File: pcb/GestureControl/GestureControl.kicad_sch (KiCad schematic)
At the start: 71 parts, among them J1 Conn_01x04_I2I-LCD, J2 BATT, J3 Conn_01x08, J4 Conn_01x06, J5 Conn_01x10, J6 Conn_01x08, SW1 SW1, SW2 SW2, U1 AP5100_3.3, U2 AP5100_3.3

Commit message: add breakoutboard
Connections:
- net GPIOI_0: now also J5.2 (Pin_2); no longer J5.3 (Pin_3)
- net GPIOI_1: now also J5.3 (Pin_3); no longer J5.4 (Pin_4)
- net GPIOI_2: now also J5.4 (Pin_4); no longer J5.5 (Pin_5)
- net GPIOI_3: now also J5.5 (Pin_5); no longer J5.6 (Pin_6)
- net XSHUT_0: now also J3.8 (Pin_8); no longer J4.1 (Pin_1)
- net XSHUT_1: now also J4.1 (Pin_1); no longer J4.2 (Pin_2)
- net XSHUT_2: now also J4.2 (Pin_2); no longer J4.3 (Pin_3)
- net XSHUT_3: now also J4.3 (Pin_3); no longer J4.4 (Pin_4)
- new net GPIOI_4: J5.6 (Pin_6)
- new net XSHUT_4: J4.4 (Pin_4)

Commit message: add docs
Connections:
- net LED_5 is gone; now on net LED_4: J6.3 (Pin_3), R5.2
- net LED_1: now also J6.6 (Pin_6), R2.2; no longer J6.7 (Pin_7), R1.2
- net LED_2: now also J6.5 (Pin_5), R3.2; no longer J6.6 (Pin_6), R2.2
- net LED_3: now also J6.4 (Pin_4), R4.2; no longer J6.5 (Pin_5), R3.2
- net LED_4: no longer J6.4 (Pin_4), R4.2
- new net LED_0: J6.7 (Pin_7), R1.2
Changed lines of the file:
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@@
     )
   )
-  (global_label "LED_1" (shape input) (at 26.67 31.75 180) (fields_autoplaced)
+  (global_label "LED_0" (shape input) (at 26.67 31.75 180) (fields_autoplaced)
     (effects (font (size 1.27 1.27)) (justify right))
-    (property "Intersheet References" "${INTERSHEET_REFS}" (id 0) (at 0 0 0)
-      (effects (font (size 1.27 1.27)) hide)
+    (property "Intersheet References" "${INTERSHEET_REFS}" (id 0) (at 18.7215 31.6706 0)
+      (effects (font (size 1.27 1.27)) (justify right) hide)
     )
   )
@@
     )
   )
-  (global_label "LED_4" (shape input) (at 242.57 129.54 0) (fields_autoplaced)
+  (global_label "LED_3" (shape input) (at 242.57 129.54 0) (fields_autoplaced)
     (effects (font (size 1.27 1.27)) (justify left))
-    (property "Intersheet References" "${INTERSHEET_REFS}" (id 0) (at 0 0 0)
-      (effects (font (size 1.27 1.27)) hide)
+    (property "Intersheet References" "${INTERSHEET_REFS}" (id 0) (at 250.5185 129.4606 0)
+      (effects (font (size 1.27 1.27)) (justify left) hide)
     )
   )
@@
     )
   )
-  (global_label "LED_4" (shape input) (at 26.67 66.04 180) (fields_autoplaced)
+  (global_label "LED_3" (shape input) (at 26.67 66.04 180) (fields_autoplaced)
     (effects (font (size 1.27 1.27)) (justify right))
-    (property "Intersheet References" "${INTERSHEET_REFS}" (id 0) (at 0 0 0)
-      (effects (font (size 1.27 1.27)) hide)
+    (property "Intersheet References" "${INTERSHEET_REFS}" (id 0) (at 18.7215 65.9606 0)
+      (effects (font (size 1.27 1.27)) (justify right) hide)
     )
   )
@@
     )
   )
-  (global_label "LED_3" (shape input) (at 242.57 127 0) (fields_autoplaced)
+  (global_label "LED_2" (shape input) (at 242.57 127 0) (fields_autoplaced)
     (effects (font (size 1.27 1.27)) (justify left))
-    (property "Intersheet References" "${INTERSHEET_REFS}" (id 0) (at 0 0 0)
-      (effects (font (size 1.27 1.27)) hide)
+    (property "Intersheet References" "${INTERSHEET_REFS}" (id 0) (at 250.5185 126.9206 0)
+      (effects (font (size 1.27 1.27)) (justify left) hide)
     )
   )
@@
     )
   )
-  (global_label "LED_2" (shape input) (at 242.57 124.46 0) (fields_autoplaced)
+  (global_label "LED_1" (shape input) (at 242.57 124.46 0) (fields_autoplaced)
     (effects (font (size 1.27 1.27)) (justify left))
-    (property "Intersheet References" "${INTERSHEET_REFS}" (id 0) (at 0 0 0)
-      (effects (font (size 1.27 1.27)) hide)
+    (property "Intersheet References" "${INTERSHEET_REFS}" (id 0) (at 250.5185 124.3806 0)
+      (effects (font (size 1.27 1.27)) (justify left) hide)
     )
   )
@@
     )
   )
-  (global_label "LED_5" (shape input) (at 242.57 132.08 0) (fields_autoplaced)
+  (global_label "LED_4" (shape input) (at 242.57 132.08 0) (fields_autoplaced)
     (effects (font (size 1.27 1.27)) (justify left))
-    (property "Intersheet References" "${INTERSHEET_REFS}" (id 0) (at 0 0 0)
-      (effects (font (size 1.27 1.27)) hide)
+    (property "Intersheet References" "${INTERSHEET_REFS}" (id 0) (at 250.5185 132.0006 0)
+      (effects (font (size 1.27 1.27)) (justify left) hide)
     )
   )
-  (global_label "LED_3" (shape input) (at 26.67 54.61 180) (fields_autoplaced)
+  (global_label "LED_2" (shape input) (at 26.67 54.61 180) (fields_autoplaced)
     (effects (font (size 1.27 1.27)) (justify right))
-    (property "Intersheet References" "${INTERSHEET_REFS}" (id 0) (at 0 0 0)
-      (effects (font (size 1.27 1.27)) hide)
+    (property "Intersheet References" "${INTERSHEET_REFS}" (id 0) (at 18.7215 54.5306 0)
+      (effects (font (size 1.27 1.27)) (justify right) hide)
     )
   )
-  (global_label "LED_1" (shape input) (at 242.57 121.92 0) (fields_autoplaced)
+  (global_label "LED_0" (shape input) (at 242.57 121.92 0) (fields_autoplaced)
     (effects (font (size 1.27 1.27)) (justify left))
-    (property "Intersheet References" "${INTERSHEET_REFS}" (id 0) (at 0 0 0)
-      (effects (font (size 1.27 1.27)) hide)
+    (property "Intersheet References" "${INTERSHEET_REFS}" (id 0) (at 250.5185 121.8406 0)
+      (effects (font (size 1.27 1.27)) (justify left) hide)
     )
   )
@@
     )
   )
-  (global_label "LED_2" (shape input) (at 26.67 43.18 180) (fields_autoplaced)
+  (global_label "LED_1" (shape input) (at 26.67 43.18 180) (fields_autoplaced)
     (effects (font (size 1.27 1.27)) (justify right))
-    (property "Intersheet References" "${INTERSHEET_REFS}" (id 0) (at 0 0 0)
-      (effects (font (size 1.27 1.27)) hide)
+    (property "Intersheet References" "${INTERSHEET_REFS}" (id 0) (at 18.7215 43.1006 0)
+      (effects (font (size 1.27 1.27)) (justify right) hide)
     )
   )
@@
     )
   )
-  (global_label "LED_5" (shape input) (at 26.67 77.47 180) (fields_autoplaced)
+  (global_label "LED_4" (shape input) (at 26.67 77.47 180) (fields_autoplaced)
     (effects (font (size 1.27 1.27)) (justify right))
-    (property "Intersheet References" "${INTERSHEET_REFS}" (id 0) (at 0 0 0)
-      (effects (font (size 1.27 1.27)) hide)
+    (property "Intersheet References" "${INTERSHEET_REFS}" (id 0) (at 18.7215 77.3906 0)
+      (effects (font (size 1.27 1.27)) (justify right) hide)
     )
   )

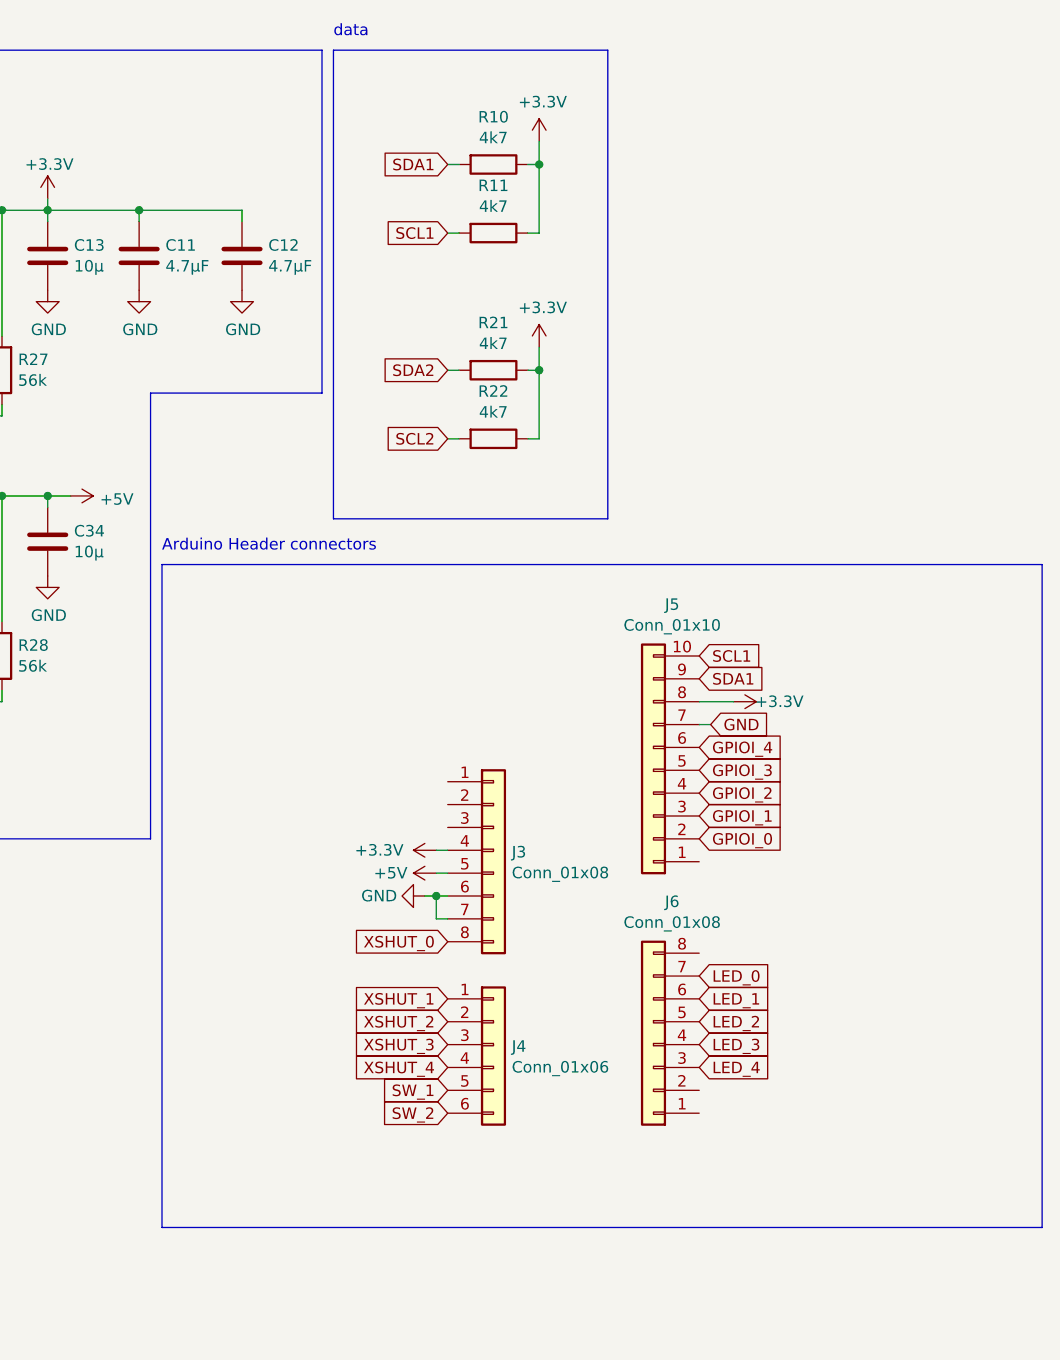
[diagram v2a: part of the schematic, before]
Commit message: ADD RC op I2C
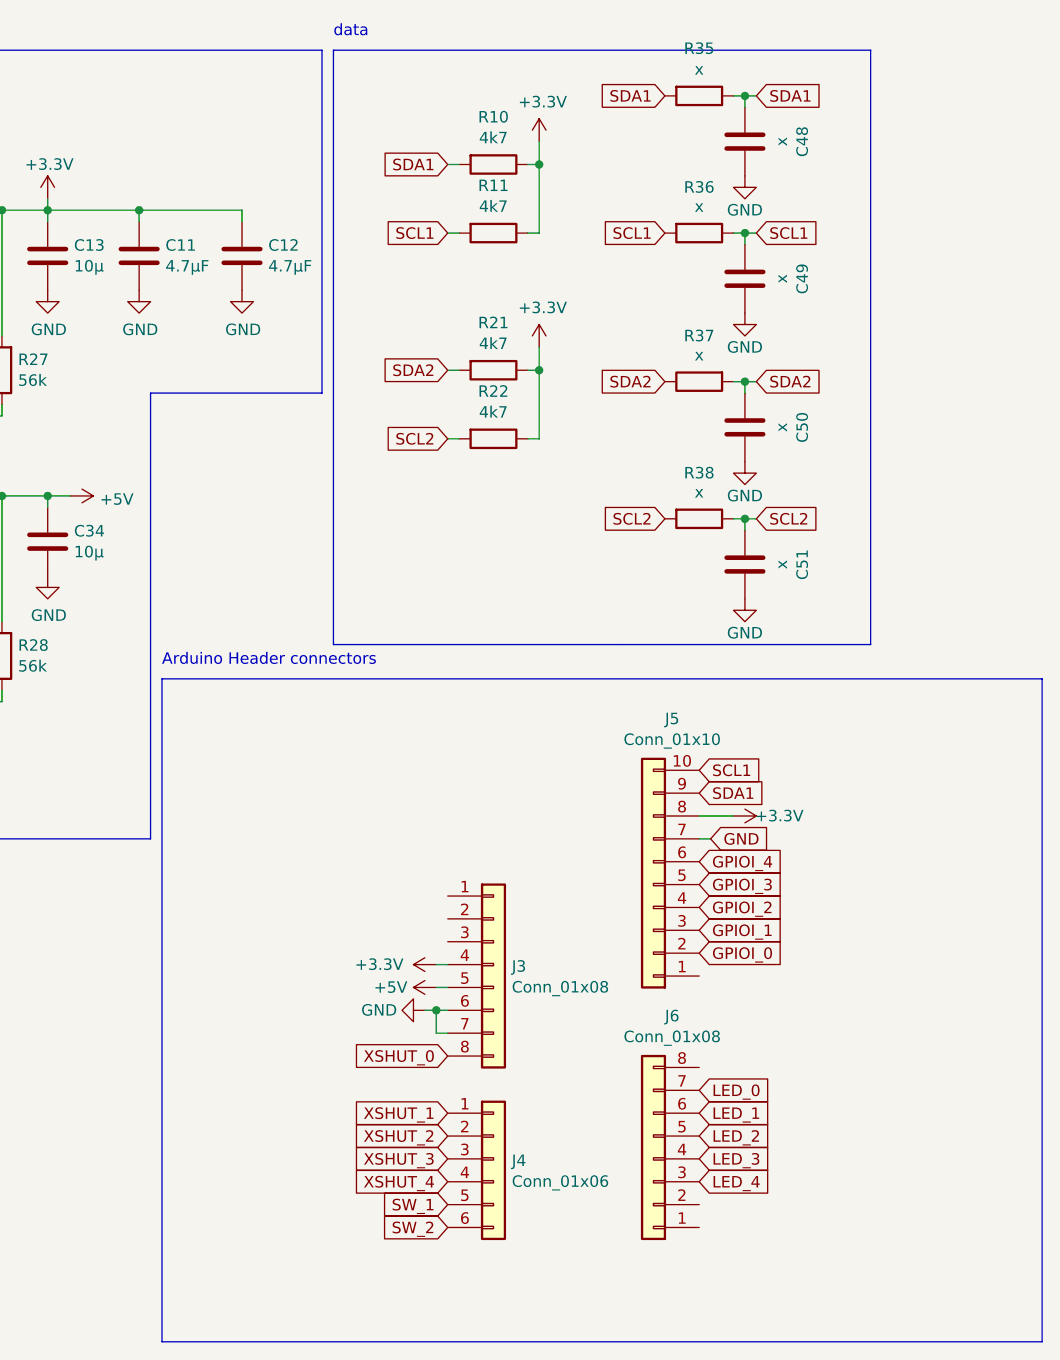
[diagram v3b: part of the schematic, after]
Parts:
- added C48, C49, C50, C51: x, Capacitor_SMD:C_0805_2012Metric_Pad1.18x1.45mm_HandSolder, symbol Device:C
- added R35, R36, R37, R38: x, Resistor_SMD:R_0805_2012Metric_Pad1.20x1.40mm_HandSolder, symbol Device:R
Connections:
- net GND: now also C48.1, C49.1, C50.1, C51.1
- net SCL1: now also C49.2, R36.1, R36.2
- net SCL2: now also C51.2, R38.1, R38.2
- net SDA1: now also C48.2, R35.1, R35.2
- net SDA2: now also C50.2, R37.1, R37.2
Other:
- moved on the sheet: J3, J4, J5, J6

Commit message: add PCBV0.3
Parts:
- removed J3, J6: Conn_01x08, Connector_PinHeader_2.54mm:PinHeader_1x08_P2.54mm_Vertical, symbol Connector_Generic:Conn_01x08
- removed J4: Conn_01x06, Connector_PinHeader_2.54mm:PinHeader_1x06_P2.54mm_Vertical, symbol Connector_Generic:Conn_01x06
- removed J5: Conn_01x10, Connector_PinHeader_2.54mm:PinHeader_1x10_P2.54mm_Vertical, symbol Connector_Generic:Conn_01x10
- added J24, J25: Conn_02x19_Odd_Even, Connector_PinSocket_2.54mm:PinSocket_2x19_P2.54mm_Vertical, symbol Connector_Generic:Conn_02x19_Odd_Even
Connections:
- net +3V3: now also J24.16 (Pin_16), J25.7 (Pin_7)
- net +5V: now also J24.18 (Pin_18)
- net GND: now also J24.19 (Pin_19), J24.20 (Pin_20), J24.22 (Pin_22), J24.8 (Pin_8), J25.20 (Pin_20), J25.32 (Pin_32), J25.9 (Pin_9)
- net GPIOI_0: now also J25.2 (Pin_2)
- net GPIOI_1: now also J25.21 (Pin_21)
- net GPIOI_2: now also J25.19 (Pin_19)
- net GPIOI_3: now also J25.17 (Pin_17)
- net GPIOI_4: now also J25.11 (Pin_11)
- net LED_0: now also J25.25 (Pin_25)
- net LED_1: now also J25.27 (Pin_27)
- net LED_2: now also J25.29 (Pin_29)
- net LED_3: now also J25.15 (Pin_15)
- net LED_4: now also J25.33 (Pin_33)
- net SCL1: now also J25.3 (Pin_3)
- net SCL2: now also J25.23 (Pin_23)
- net SDA1: now also J25.5 (Pin_5)
- net SDA2: now also J25.1 (Pin_1)
- net SW_1: now also J24.36 (Pin_36)
- net SW_2: now also J24.38 (Pin_38)
- net XSHUT_0: now also J25.13 (Pin_13)
- net XSHUT_1: now also J24.28 (Pin_28)
- net XSHUT_2: now also J24.30 (Pin_30)
- net XSHUT_3: now also J24.32 (Pin_32)
- net XSHUT_4: now also J24.34 (Pin_34)
- no-connect marks 0 -> 8
